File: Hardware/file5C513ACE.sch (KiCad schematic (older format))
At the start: 70 parts, among them J1 GATE_2, J2 GATE_3, J3 GATE_1, Q1 MMBT3904, Q2 MMBT3904, Q3 MMBT3904, SW1 Frequency Adjust, SW10 PROG, SW11 PROG, SW2 PROG, SW3 PROG, SW4 PROG, SW5 PROG, SW6 PROG, SW7 RST, SW8 PROG, SW9 PROG, U1 TLC5947DAP

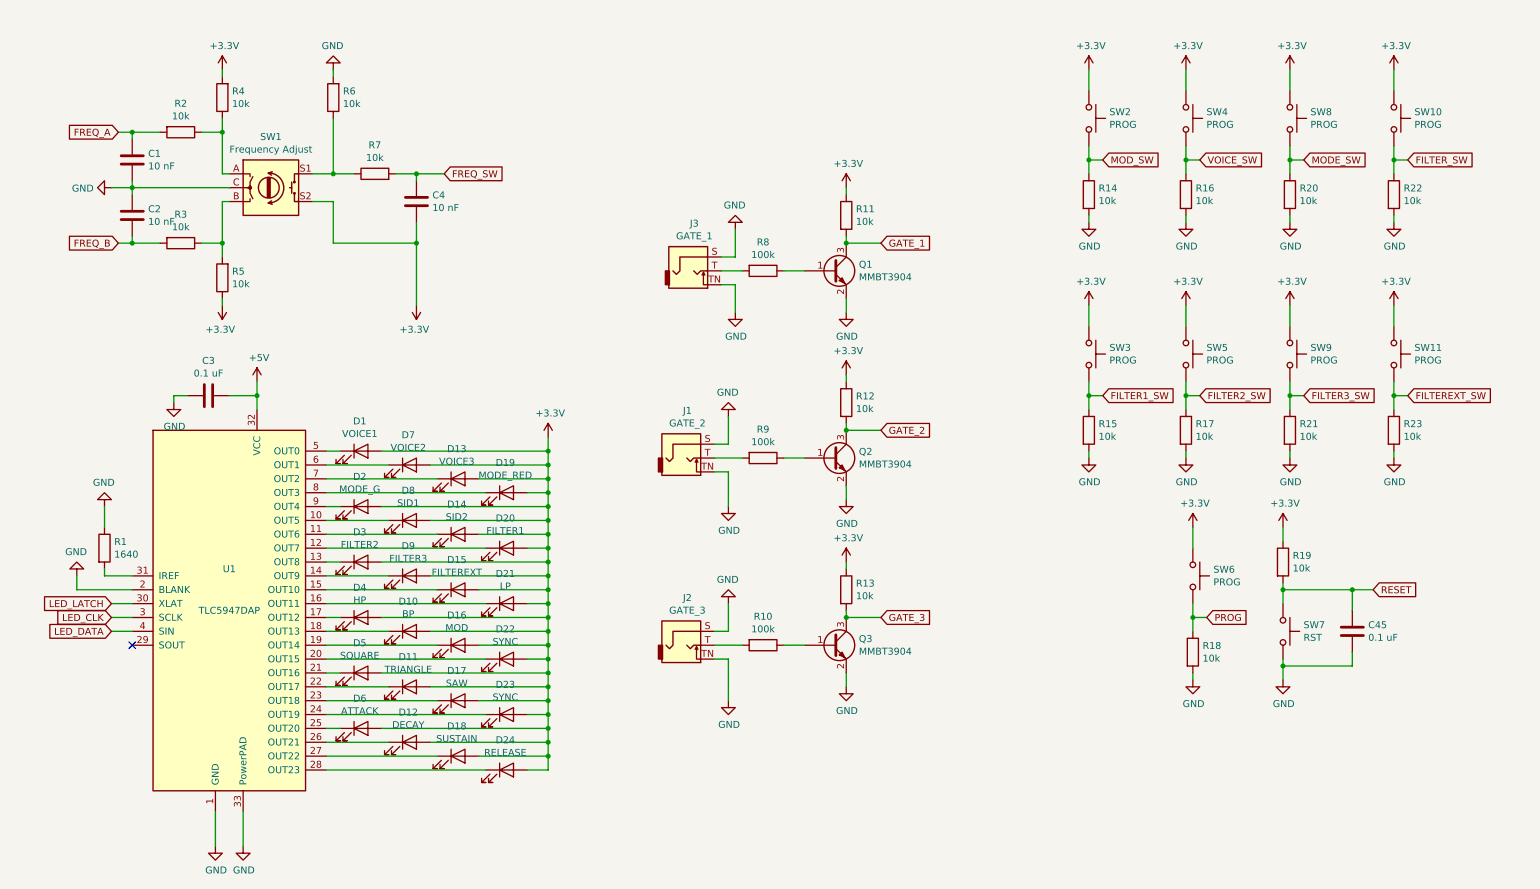
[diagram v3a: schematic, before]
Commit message: Finished assigning footprints
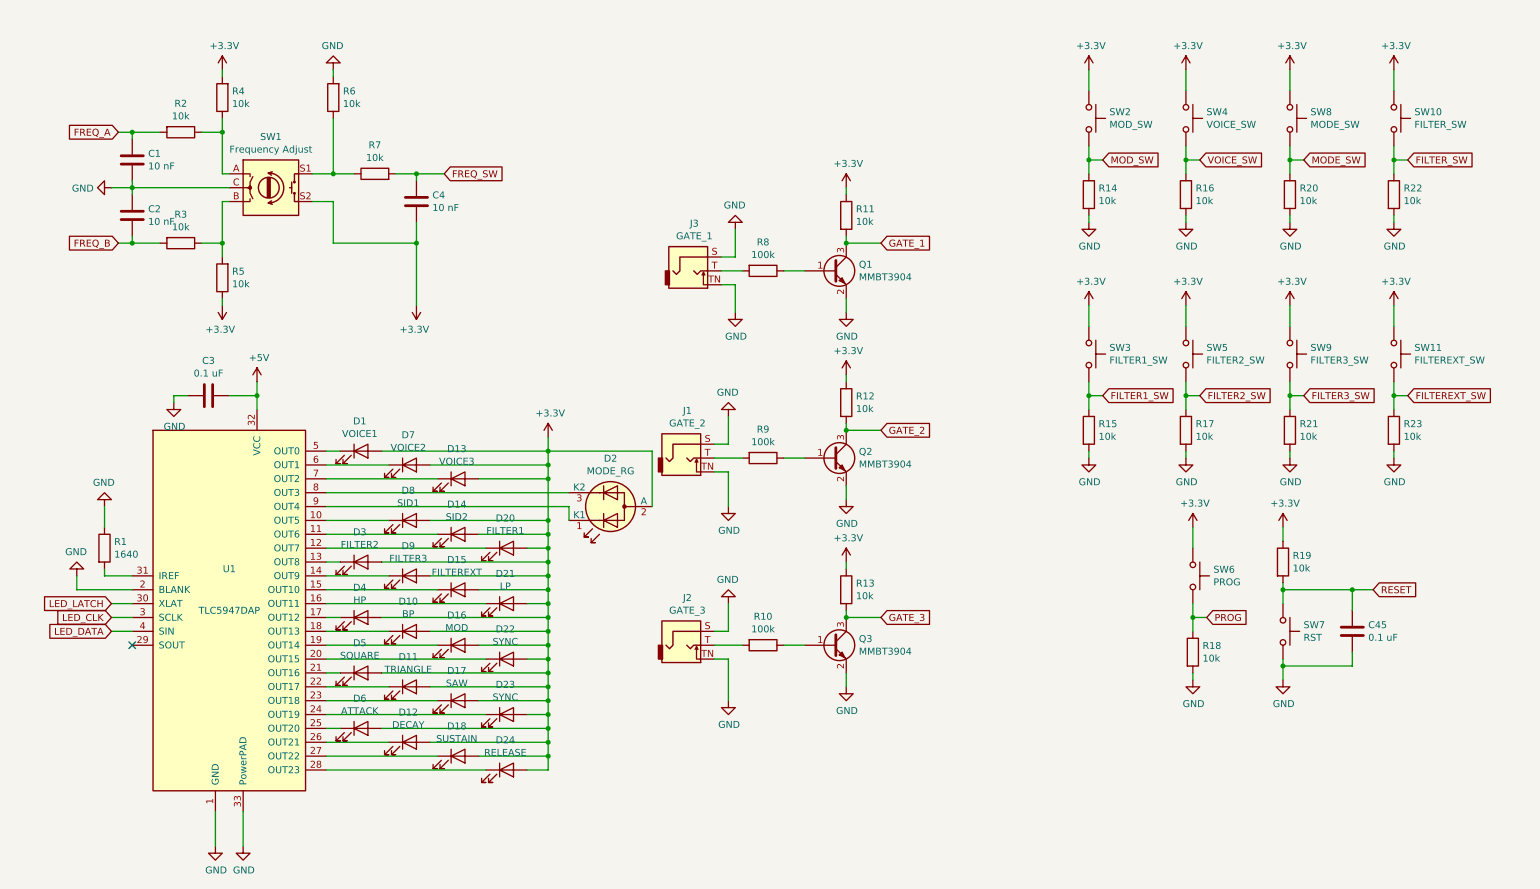
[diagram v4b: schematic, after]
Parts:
- removed D19: MODE_RED, symbol Device:LED
- removed D2: MODE_G, symbol Device:LED
- added D2: MODE_RG, LED_THT:LED_D3.0mm-3, symbol Device:LED_Dual_CAC
- D1, D10, D11, D12, D13, D14, D15, D16, D17, D18, D20, D21, D22, D23, D24, D3, D4, D5, D6, D7, D8, D9: footprint (none) -> LED_THT:LED_D3.0mm
- SW1: footprint (none) -> Rotary_Encoder:RotaryEncoder_Alps_EC12E-Switch_Vertical_H20mm_CircularMountingHoles
- SW10: value PROG -> FILTER_SW; footprint (none) -> Button_Switch_THT:SW_PUSH_6mm_H9.5mm
- SW11: value PROG -> FILTEREXT_SW; footprint (none) -> Button_Switch_THT:SW_PUSH_6mm_H9.5mm
- SW2: value PROG -> MOD_SW; footprint (none) -> Button_Switch_THT:SW_PUSH_6mm_H9.5mm
- SW3: value PROG -> FILTER1_SW; footprint (none) -> Button_Switch_THT:SW_PUSH_6mm_H9.5mm
- SW4: value PROG -> VOICE_SW; footprint (none) -> Button_Switch_THT:SW_PUSH_6mm_H9.5mm
- SW5: value PROG -> FILTER2_SW; footprint (none) -> Button_Switch_THT:SW_PUSH_6mm_H9.5mm
- SW6, SW7: footprint (none) -> Button_Switch_SMD:SW_SPST_EVPBF
- SW8: value PROG -> MODE_SW; footprint (none) -> Button_Switch_THT:SW_PUSH_6mm_H9.5mm
- SW9: value PROG -> FILTER3_SW; footprint (none) -> Button_Switch_THT:SW_PUSH_6mm_H9.5mm
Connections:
- net +3V3: now also D2.2 (A)
- net at U1.8 (OUT3): now also D2.3 (K2)
- net at U1.9 (OUT4): now also D2.1 (K1)

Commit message: Updated schematic
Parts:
- added R22: 10k, Resistor_SMD:R_0603_1608Metric, symbol Device:R
- added SW10: SET_SW, Button_Switch_THT:SW_PUSH_6mm_H9.5mm, symbol Switch:SW_Push
- renumbered C45 to C5, D11 to D10, D12 to D11, D13 to D12, D14 to D13, D15 to D14, D16 to D15, D17 to D16, D18 to D17, D20 to D18, D21 to D19, D3 to D2, D22 to D20, D23 to D21, D24 to D22, D2 to D23, D4 to D3, D5 to D4, D6 to D5, D7 to D6, D8 to D7, D9 to D8, D10 to D9, R18 to R16, R16 to R17, R17 to R18, R22 to R23, R23 to R24, SW10 to SW11, SW11 to SW12, SW6 to SW4, SW4 to SW5, SW5 to SW6
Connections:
- net +3V3: now also SW10.1
- net GND: now also R22.2
- new net SET_SW: R22.1, SW10.2
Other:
- moved on the sheet: C5, J1, J2, J3, Q1, Q2, Q3, R10, R11, R12, R13, R16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

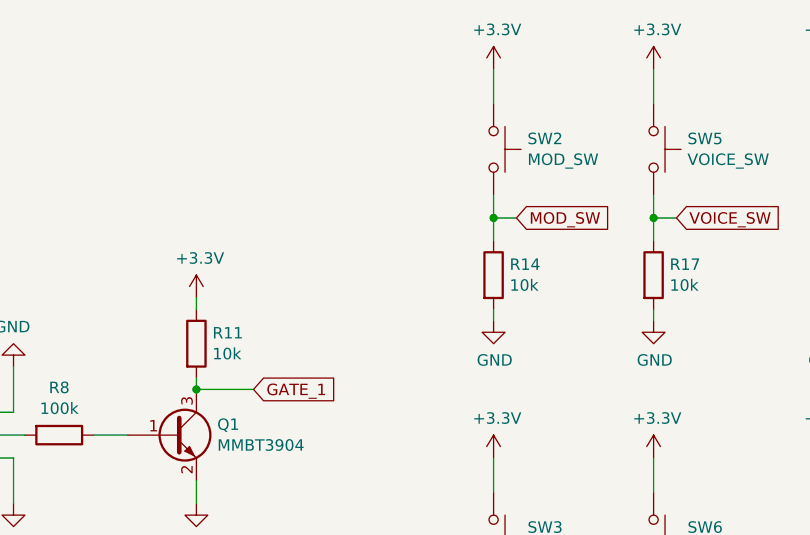
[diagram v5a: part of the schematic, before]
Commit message: Fixed footprints for new attenuverter pots
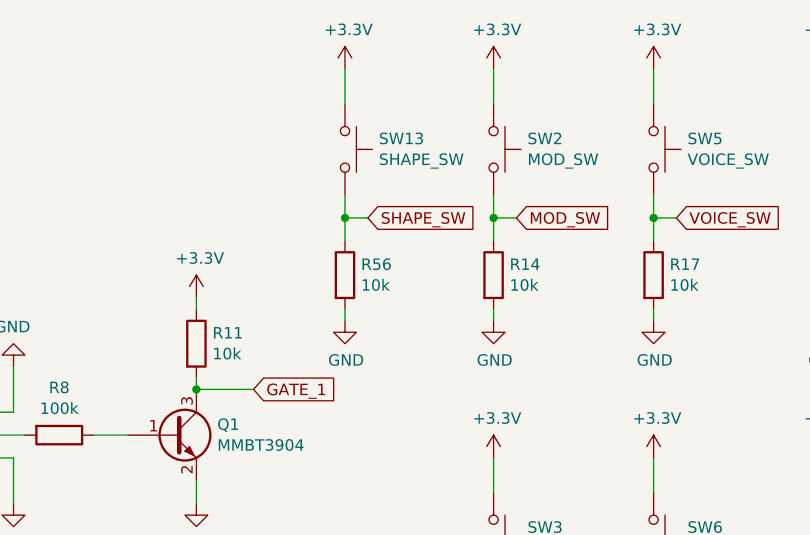
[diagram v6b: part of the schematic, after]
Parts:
- added R56: 10k, Resistor_SMD:R_0603_1608Metric, symbol Device:R
- added SW13: SHAPE_SW, Button_Switch_THT:SW_PUSH_6mm_H9.5mm, symbol Switch:SW_Push
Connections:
- net +3V3: now also SW13.1
- net GND: now also R56.2
- new net SHAPE_SW: R56.1, SW13.2
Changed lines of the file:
@@
 Wire Wire Line
 	9900 4700 9900 4800
+$Comp
+L Switch:SW_Push SW?
+U 1 1 5BFE4CDB
+P 7350 1150
+AR Path="/5C5B0294/5BFE4CDB" Ref="SW?"  Part="1"
+AR Path="/5BFD63E3/5C513ACF/5BFE4CDB" Ref="SW13"  Part="1"
+F 0 "SW13" V 7304 1298 50  0000 L CNN
+F 1 "SHAPE_SW" V 7395 1298 50  0000 L CNN
+F 2 "Button_Switch_THT:SW_PUSH_6mm_H9.5mm" H 7350 1350 50  0001 C CNN
+F 3 "" H 7350 1350 50  0001 C CNN
+	1    7350 1150
+	0    1    1    0
+$EndComp
+$Comp
+L power:GND #PWR?
+U 1 1 5BFE4CE2
+P 7350 1900
+AR Path="/5C5B0294/5BFE4CE2" Ref="#PWR?"  Part="1"
+AR Path="/5BFD63E3/5C513ACF/5BFE4CE2" Ref="#PWR0158"  Part="1"
+F 0 "#PWR0158" H 7350 1650 50  0001 C CNN
+F 1 "GND" H 7355 1727 50  0000 C CNN
+F 2 "" H 7350 1900 50  0001 C CNN
+F 3 "" H 7350 1900 50  0001 C CNN
+	1    7350 1900
+	1    0    0    -1
+$EndComp
+$Comp
+L Device:R R?
+U 1 1 5BFE4CE8
+P 7350 1700
+AR Path="/5C5B0294/5BFE4CE8" Ref="R?"  Part="1"
+AR Path="/5BFD63E3/5C513ACF/5BFE4CE8" Ref="R56"  Part="1"
+F 0 "R56" H 7420 1746 50  0000 L CNN
+F 1 "10k" H 7420 1655 50  0000 L CNN
+F 2 "Resistor_SMD:R_0603_1608Metric" V 7280 1700 50  0001 C CNN
+F 3 "~" H 7350 1700 50  0001 C CNN
+	1    7350 1700
+	1    0    0    -1
+$EndComp
+$Comp
+L power:+3.3V #PWR?
+U 1 1 5BFE4CEF
+P 7350 800
+AR Path="/5C5B0294/5BFE4CEF" Ref="#PWR?"  Part="1"
+AR Path="/5BFD63E3/5C513ACF/5BFE4CEF" Ref="#PWR0157"  Part="1"
+F 0 "#PWR0157" H 7350 650 50  0001 C CNN
+F 1 "+3.3V" H 7365 973 50  0000 C CNN
+F 2 "" H 7350 800 50  0001 C CNN
+F 3 "" H 7350 800 50  0001 C CNN
+	1    7350 800
+	1    0    0    -1
+$EndComp
+Wire Wire Line
+	7350 800  7350 950
+Wire Wire Line
+	7350 1850 7350 1900
+Wire Wire Line
+	7350 1350 7350 1450
+Text GLabel 7450 1450 2    50   Input ~ 0
+SHAPE_SW
+Wire Wire Line
+	7450 1450 7350 1450
+Connection ~ 7350 1450
+Wire Wire Line
+	7350 1450 7350 1550
 $EndSCHEMATC

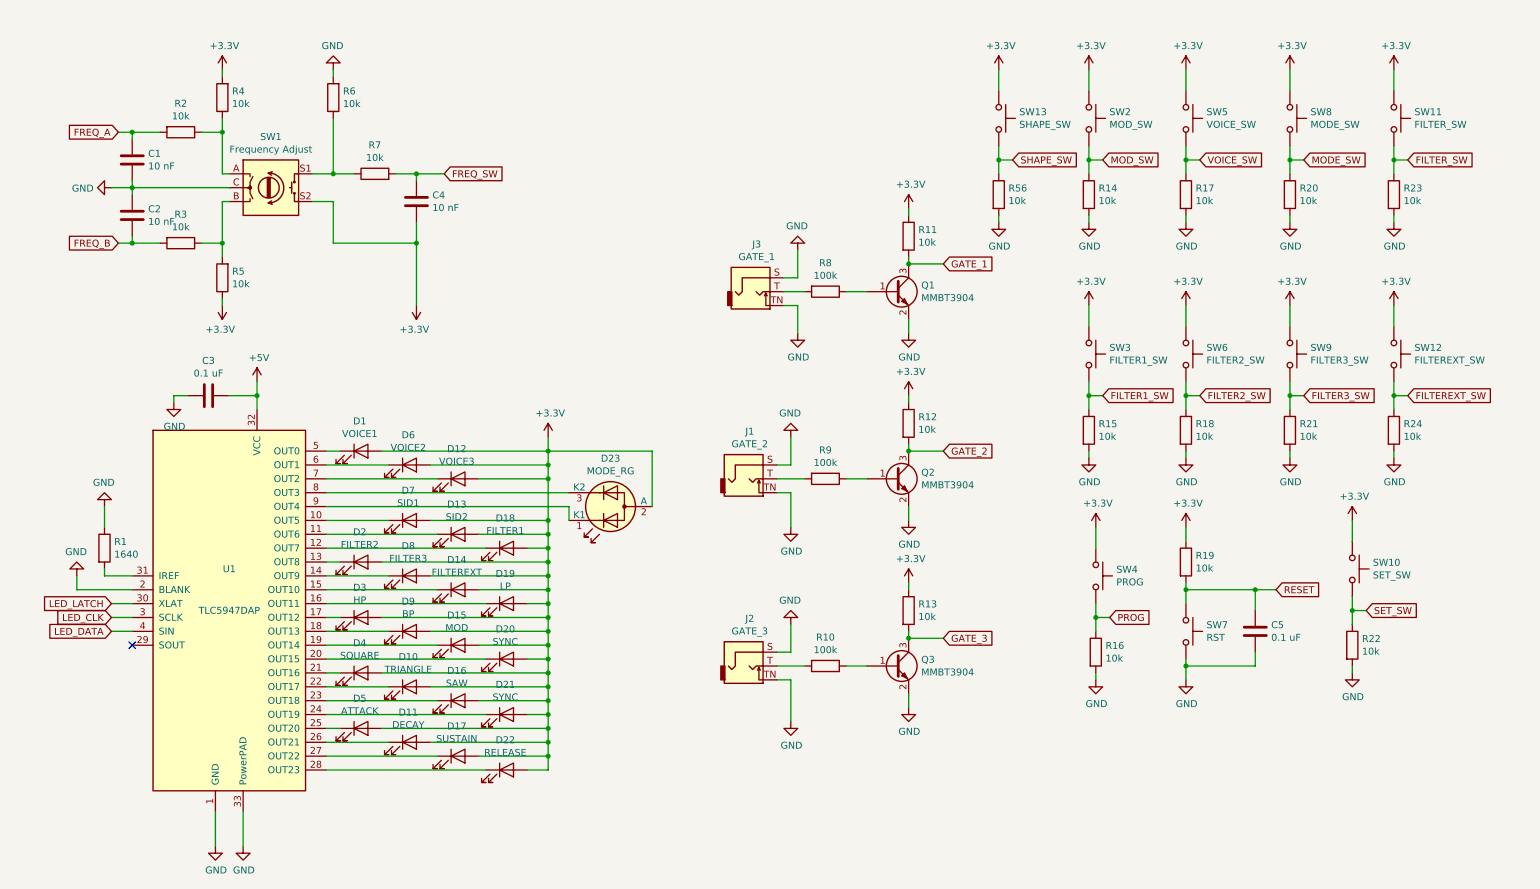
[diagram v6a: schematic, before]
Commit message: Seperated two board with headers
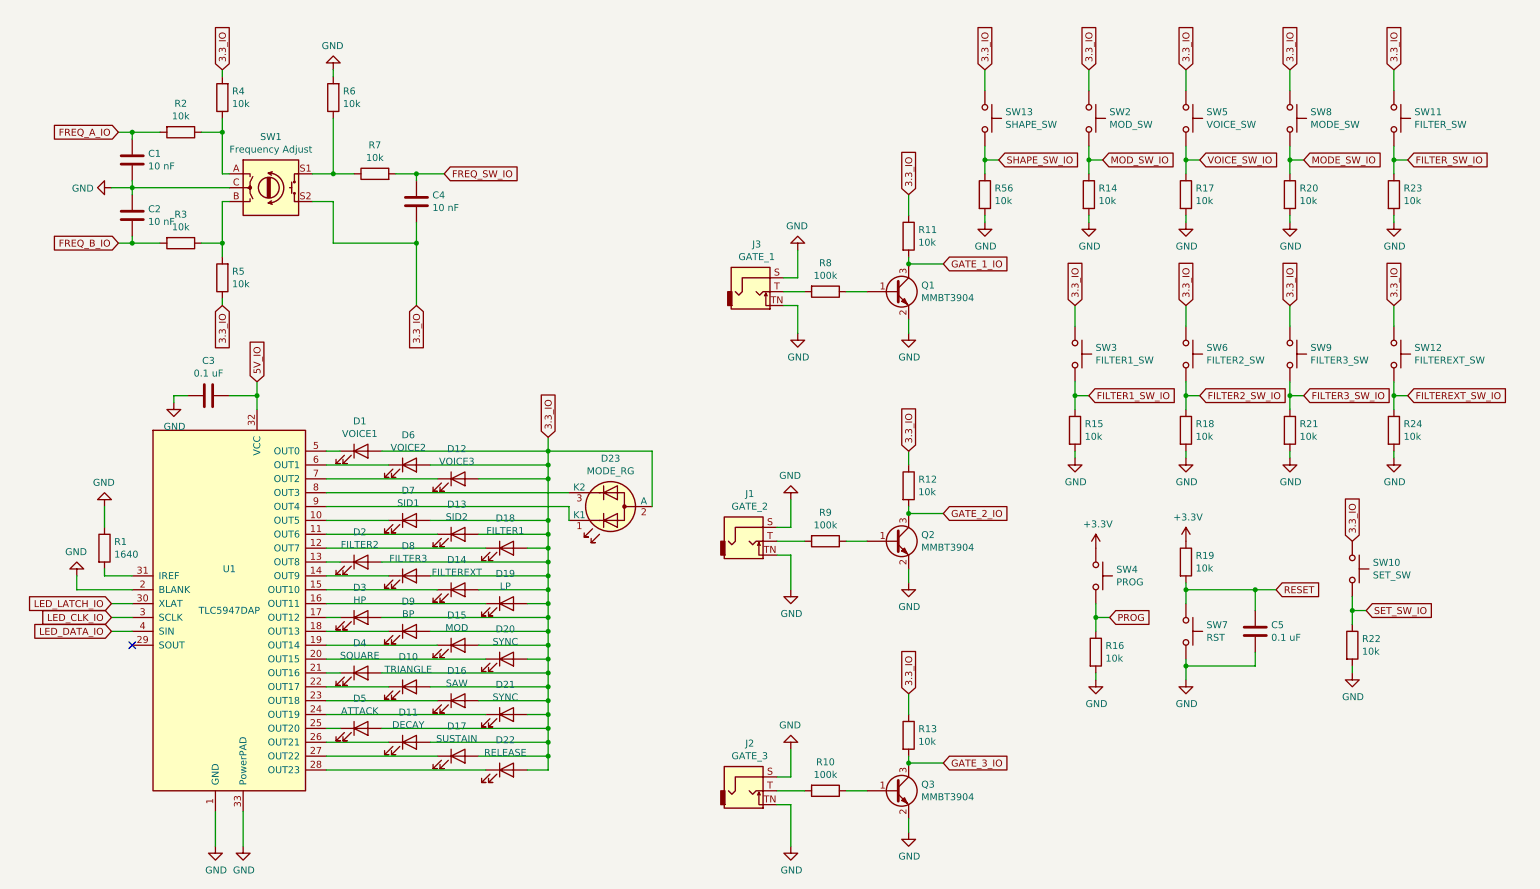
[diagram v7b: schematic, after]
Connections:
- net +3V3: no longer C4.2, D1.2 (A), D10.2 (A), D11.2 (A), D12.2 (A), D13.2 (A), D14.2 (A), D15.2 (A), D16.2 (A), D17.2 (A), D18.2 (A), D19.2 (A), D2.2 (A), D20.2 (A), D21.2 (A), D22.2 (A), D23.2 (A), D3.2 (A), D4.2 (A), D5.2 (A), D6.2 (A), D7.2 (A), D8.2 (A), D9.2 (A), R11.1, R12.1, R13.1, R4.2, R5.1, SW1.S2, SW10.1, SW11.1, SW12.1, SW13.1, SW2.1, SW3.1, SW5.1, SW6.1, SW8.1, SW9.1
- net +5V renamed 5V_IO
- net FILTER1_SW renamed FILTER1_SW_IO
- net FILTER2_SW renamed FILTER2_SW_IO
- net FILTER3_SW renamed FILTER3_SW_IO
- net FILTEREXT_SW renamed FILTEREXT_SW_IO
- net FILTER_SW renamed FILTER_SW_IO
- net FREQ_A renamed FREQ_A_IO
- net FREQ_B renamed FREQ_B_IO
- net FREQ_SW renamed FREQ_SW_IO
- net GATE_1 renamed GATE_1_IO
- net GATE_2 renamed GATE_2_IO
- net GATE_3 renamed GATE_3_IO
- net LED_CLK renamed LED_CLK_IO
- net LED_DATA renamed LED_DATA_IO
- net LED_LATCH renamed LED_LATCH_IO
- net MODE_SW renamed MODE_SW_IO
- net MOD_SW renamed MOD_SW_IO
- net SET_SW renamed SET_SW_IO
- net SHAPE_SW renamed SHAPE_SW_IO
- net VOICE_SW renamed VOICE_SW_IO
- new net 3.3_IO: C4.2, D1.2 (A), D10.2 (A), D11.2 (A), D12.2 (A), D13.2 (A), D14.2 (A), D15.2 (A), D16.2 (A), D17.2 (A), D18.2 (A), D19.2 (A), D2.2 (A), D20.2 (A), D21.2 (A), D22.2 (A), D23.2 (A), D3.2 (A), D4.2 (A), D5.2 (A), D6.2 (A), D7.2 (A), D8.2 (A), D9.2 (A), R11.1, R12.1, R13.1, R4.2, R5.1, SW1.S2, SW10.1, SW11.1, SW12.1, SW13.1, SW2.1, SW3.1, SW5.1, SW6.1, SW8.1, SW9.1
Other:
- moved on the sheet: J1, J2, Q2, Q3, R10, R12, R13, R15, R56, R9, SW13, SW3

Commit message: Updated ADSR sliders
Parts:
- removed D11: DECAY, LED_THT:LED_D3.0mm, symbol Device:LED
- removed D17: SUSTAIN, LED_THT:LED_D3.0mm, symbol Device:LED
- removed D22: RELEASE, LED_THT:LED_D3.0mm, symbol Device:LED
- removed D5: ATTACK, LED_THT:LED_D3.0mm, symbol Device:LED
- added RV5: ATTACK, Potentiometer_THT:Potentiometer_Bourns_PTL20_Single_Slide, symbol SID_Parts:BOURNS_PTL
- added RV6: DECAY, Potentiometer_THT:Potentiometer_Bourns_PTL20_Single_Slide, symbol SID_Parts:BOURNS_PTL
- added RV7: SUSTAIN, Potentiometer_THT:Potentiometer_Bourns_PTL20_Single_Slide, symbol SID_Parts:BOURNS_PTL
- added RV8: RELEASE, Potentiometer_THT:Potentiometer_Bourns_PTL20_Single_Slide, symbol SID_Parts:BOURNS_PTL
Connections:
- net 3.3_IO: now also RV5.B (A), RV6.B (A), RV7.B (A), RV8.B (A)
- net at U1.25 (OUT20): now also RV5.E (K)
- net at U1.26 (OUT21): now also RV6.E (K)
- net at U1.27 (OUT22): now also RV7.E (K)
- net at U1.28 (OUT23): now also RV8.E (K)
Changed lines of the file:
@@
-	1    0    0    -1
-$EndComp
-$Comp
-L Device:LED D?
-U 1 1 5C6023D5
-P 2750 5550
-AR Path="/5BFD63E3/5C6023D5" Ref="D?"  Part="1"
-AR Path="/5BFD63E3/5C513ACF/5C6023D5" Ref="D5"  Part="1"
-F 0 "D5" H 2741 5766 50  0000 C CNN
-F 1 "ATTACK" H 2741 5675 50  0000 C CNN
-F 2 "LED_THT:LED_D3.0mm" H 2750 5550 50  0001 C CNN
-F 3 "~" H 2750 5550 50  0001 C CNN
-	1    2750 5550
-	1    0    0    -1
-$EndComp
-$Comp
-L Device:LED D?
-U 1 1 5C6023DC
-P 3100 5650
-AR Path="/5BFD63E3/5C6023DC" Ref="D?"  Part="1"
-AR Path="/5BFD63E3/5C513ACF/5C6023DC" Ref="D11"  Part="1"
-F 0 "D11" H 3091 5866 50  0000 C CNN
-F 1 "DECAY" H 3091 5775 50  0000 C CNN
-F 2 "LED_THT:LED_D3.0mm" H 3100 5650 50  0001 C CNN
-F 3 "~" H 3100 5650 50  0001 C CNN
-	1    3100 5650
-	1    0    0    -1
-$EndComp
-$Comp
-L Device:LED D?
-U 1 1 5C6023E3
-P 3450 5750
-AR Path="/5BFD63E3/5C6023E3" Ref="D?"  Part="1"
-AR Path="/5BFD63E3/5C513ACF/5C6023E3" Ref="D17"  Part="1"
-F 0 "D17" H 3441 5966 50  0000 C CNN
-F 1 "SUSTAIN" H 3441 5875 50  0000 C CNN
-F 2 "LED_THT:LED_D3.0mm" H 3450 5750 50  0001 C CNN
-F 3 "~" H 3450 5750 50  0001 C CNN
-	1    3450 5750
-	1    0    0    -1
-$EndComp
-$Comp
-L Device:LED D?
-U 1 1 5C6023EA
-P 3800 5850
-AR Path="/5BFD63E3/5C6023EA" Ref="D?"  Part="1"
-AR Path="/5BFD63E3/5C513ACF/5C6023EA" Ref="D22"  Part="1"
-F 0 "D22" H 3791 6066 50  0000 C CNN
-F 1 "RELEASE" H 3791 5975 50  0000 C CNN
-F 2 "LED_THT:LED_D3.0mm" H 3800 5850 50  0001 C CNN
-F 3 "~" H 3800 5850 50  0001 C CNN
-	1    3800 5850
 	1    0    0    -1
 $EndComp
@@
 	2500 5550 2600 5550
 Wire Wire Line
-	2500 5650 2950 5650
-Wire Wire Line
-	2500 5750 3300 5750
-Wire Wire Line
-	2500 5850 3650 5850
+	2500 5650 2650 5650
+Wire Wire Line
+	2500 5750 3000 5750
+Wire Wire Line
+	2500 5850 3350 5850
 Wire Wire Line
 	4100 3450 4100 3550
@@
 Text GLabel 4100 3450 1    50   Input ~ 0
 3.3_IO
+$Comp
+L SID_Parts:BOURNS_PTL RV?
+U 2 1 5C0B06A6
+P 2900 5500
+AR Path="/5BFD63E3/5C513EEB/5C0B06A6" Ref="RV?"  Part="2"
+AR Path="/5BFD63E3/5C513ACF/5C0B06A6" Ref="RV5"  Part="2"
+F 0 "RV5" V 2725 5341 50  0000 C CNN
+F 1 "ATTACK" V 2816 5341 50  0000 C CNN
+F 2 "Potentiometer_THT:Potentiometer_Bourns_PTL20_Single_Slide" H 2900 5500 50  0001 C CNN
+F 3 "" H 2900 5500 50  0001 C CNN
+	2    2900 5500
+	0    1    1    0
+$EndComp
+$Comp
+L SID_Parts:BOURNS_PTL RV?
+U 2 1 5C0B06AD
+P 3600 5700
+AR Path="/5BFD63E3/5C513EEB/5C0B06AD" Ref="RV?"  Part="2"
+AR Path="/5BFD63E3/5C513ACF/5C0B06AD" Ref="RV7"  Part="2"
+F 0 "RV7" V 3425 5541 50  0000 C CNN
+F 1 "SUSTAIN" V 3516 5541 50  0000 C CNN
+F 2 "Potentiometer_THT:Potentiometer_Bourns_PTL20_Single_Slide" H 3600 5700 50  0001 C CNN
+F 3 "" H 3600 5700 50  0001 C CNN
+	2    3600 5700
+	0    1    1    0
+$EndComp
+$Comp
+L SID_Parts:BOURNS_PTL RV?
+U 2 1 5C0B06B4
+P 3950 5800
+AR Path="/5BFD63E3/5C513EEB/5C0B06B4" Ref="RV?"  Part="2"
+AR Path="/5BFD63E3/5C513ACF/5C0B06B4" Ref="RV8"  Part="2"
+F 0 "RV8" V 3775 5641 50  0000 C CNN
+F 1 "RELEASE" V 3866 5641 50  0000 C CNN
+F 2 "Potentiometer_THT:Potentiometer_Bourns_PTL20_Single_Slide" H 3950 5800 50  0001 C CNN
+F 3 "" H 3950 5800 50  0001 C CNN
+	2    3950 5800
+	0    1    1    0
+$EndComp
+$Comp
+L SID_Parts:BOURNS_PTL RV?
+U 2 1 5C0B06BB
+P 3250 5600
+AR Path="/5BFD63E3/5C513EEB/5C0B06BB" Ref="RV?"  Part="2"
+AR Path="/5BFD63E3/5C513ACF/5C0B06BB" Ref="RV6"  Part="2"
+F 0 "RV6" V 3075 5441 50  0000 C CNN
+F 1 "DECAY" V 3166 5441 50  0000 C CNN
+F 2 "Potentiometer_THT:Potentiometer_Bourns_PTL20_Single_Slide" H 3250 5600 50  0001 C CNN
+F 3 "" H 3250 5600 50  0001 C CNN
+	2    3250 5600
+	0    1    1    0
+$EndComp
+Connection ~ 2650 5650
+Wire Wire Line
+	2650 5650 2950 5650
+Connection ~ 3000 5750
+Wire Wire Line
+	3000 5750 3300 5750
+Connection ~ 3350 5850
+Wire Wire Line
+	3350 5850 3650 5850
 $EndSCHEMATC
